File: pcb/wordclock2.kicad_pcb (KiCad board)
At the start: 2 copper layers, 130 x 30 mm, 57 parts, among them J1 Jack-DC, J2 CONN_02X05, J3 Micro_SD_Card_Det, J4 USB_OTG, J5 CONN_01X03, J6 CONN_01X03, Q1 FDS6890A, SW1 SW_Push, SW2 SW_Push, SW3 SW_Push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

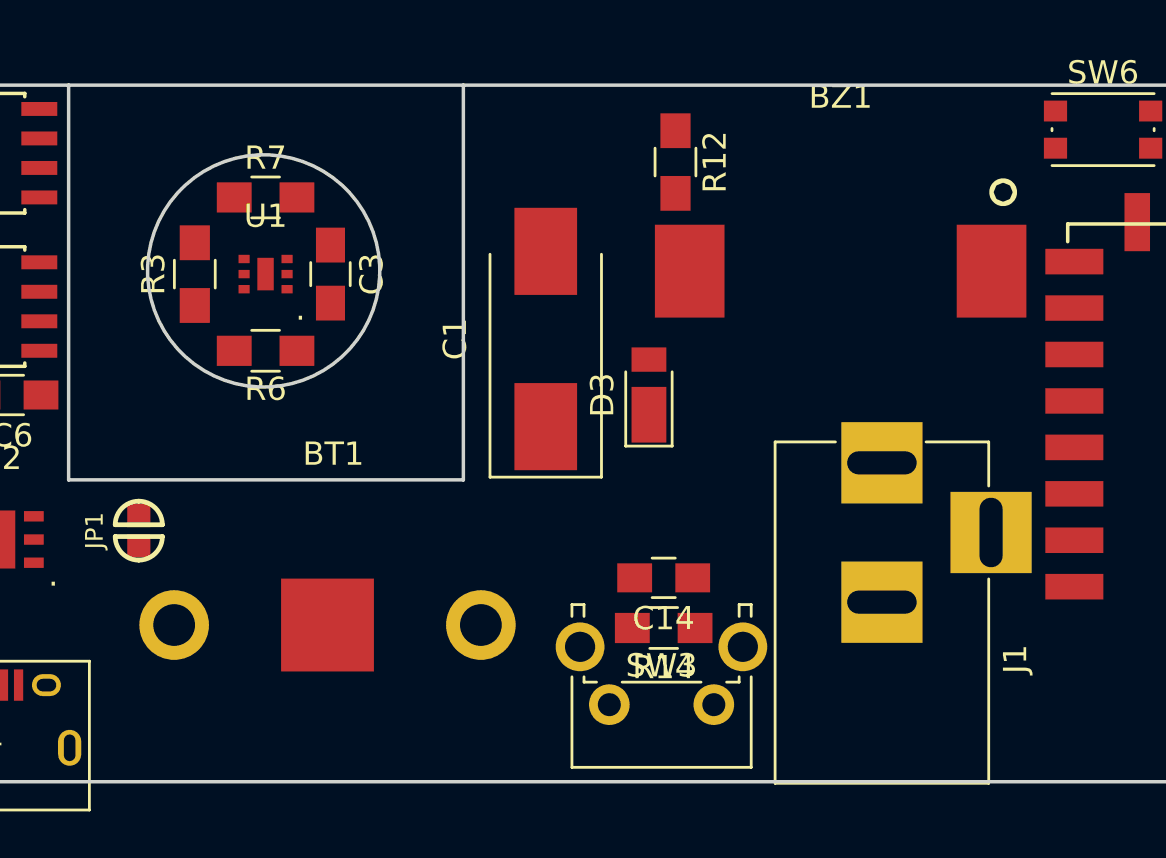
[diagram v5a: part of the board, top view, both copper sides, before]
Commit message: smaller battery mount
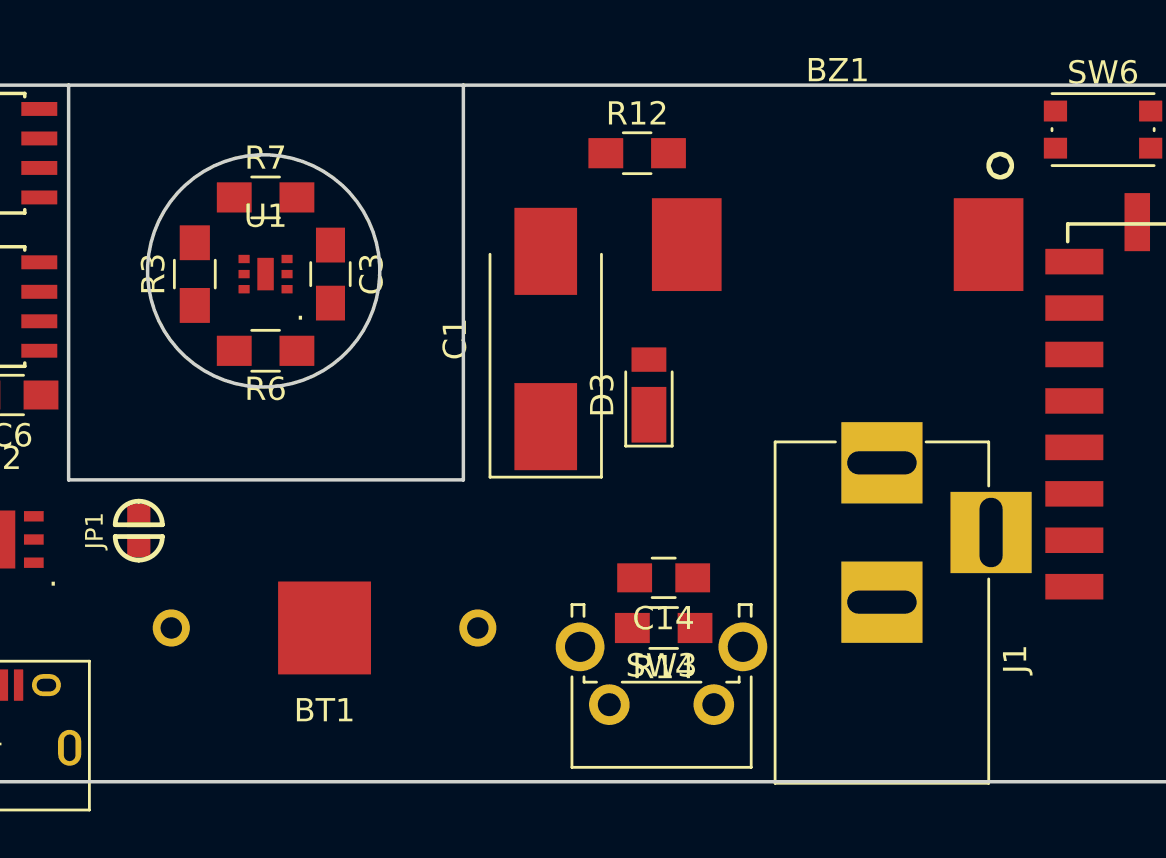
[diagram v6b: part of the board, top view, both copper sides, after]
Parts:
- BT1: footprint wordclockFB:LR44 -> wordclockFB:BK-890
- moved R12 1.69 mm to (164.1, 82.9), turned to 0 degrees
- moved BZ1 1.15 mm to (172.7, 86.9)
- moved BT1 0.18 mm to (150.6, 103.4)
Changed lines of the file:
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@@
   )
   (module wordclockFB:PKLCS1212E (layer F.Cu)
-    (at 172.847 88.011)
+    (at 172.72 86.868)
     (fp_text reference BZ1 (at 0 -7.5) (layer F.SilkS)
       (effects (font (size 1 1) (thickness 0.15)))
@@
   )
   (module Resistors_SMD:R_0805_HandSoldering (layer F.Cu)
-    (at 165.735 83.312 270)
+    (at 164.084 82.931)
     (descr "Resistor SMD 0805, hand soldering")
     (tags "resistor 0805")
     (attr smd)
-    (fp_text reference R12 (at 0 -1.7 270) (layer F.SilkS)
-      (effects (font (size 1 1) (thickness 0.15)))
-    )
-    (fp_text value 1k (at 0 1.75 270) (layer F.Fab)
-      (effects (font (size 1 1) (thickness 0.15)))
-    )
-    (fp_text user %R (at 0 0 270) (layer F.Fab)
+    (fp_text reference R12 (at 0 -1.7) (layer F.SilkS)
+      (effects (font (size 1 1) (thickness 0.15)))
+    )
+    (fp_text value 1k (at 0 1.75) (layer F.Fab)
+      (effects (font (size 1 1) (thickness 0.15)))
+    )
+    (fp_text user %R (at 0 0) (layer F.Fab)
       (effects (font (size 0.5 0.5) (thickness 0.075)))
     )
@@
     (fp_line (start 2.35 0.9) (end 2.35 -0.9) (layer F.CrtYd) (width 0.05))
     (fp_line (start 2.35 0.9) (end -2.35 0.9) (layer F.CrtYd) (width 0.05))
-    (pad 1 smd rect (at -1.35 0 270) (size 1.5 1.3) (layers F.Cu F.Paste F.Mask)
-      (net 3 +3V3))
-    (pad 2 smd rect (at 1.35 0 270) (size 1.5 1.3) (layers F.Cu F.Paste F.Mask)
+    (pad 1 smd rect (at -1.35 0) (size 1.5 1.3) (layers F.Cu F.Paste F.Mask)
+      (net 3 +3V3))
+    (pad 2 smd rect (at 1.35 0) (size 1.5 1.3) (layers F.Cu F.Paste F.Mask)
       (net 69 "Net-(BZ1-Pad1)"))
     (model ${KISYS3DMOD}/Resistors_SMD.3dshapes/R_0805.wrl
@@
     )
   )
-  (module wordclockFB:LR44 (layer F.Cu)
-    (at 150.749 103.251)
-    (fp_text reference BT1 (at 0.254 -7.366) (layer F.SilkS)
-      (effects (font (size 1 1) (thickness 0.15)))
-    )
-    (fp_text value Battery_Cell (at 0 7.874) (layer F.Fab)
-      (effects (font (size 1 1) (thickness 0.15)))
-    )
-    (fp_line (start -6.605 -6.07) (end -6.605 6.07) (layer F.Fab) (width 0.15))
-    (fp_line (start -6.605 6.07) (end 6.605 6.07) (layer F.Fab) (width 0.15))
-    (fp_line (start 6.605 6.07) (end 6.605 -6.07) (layer F.Fab) (width 0.15))
-    (fp_line (start 6.605 -6.07) (end -6.605 -6.07) (layer F.Fab) (width 0.15))
-    (pad 1 thru_hole circle (at -6.605 0) (size 3 3) (drill 1.8) (layers *.Cu *.Mask)
+  (module wordclockFB:BK-890 (layer F.Cu)
+    (at 150.622 103.378)
+    (fp_text reference BT1 (at 0 3.556) (layer F.SilkS)
+      (effects (font (size 1 1) (thickness 0.15)))
+    )
+    (fp_text value Battery_Cell (at 0 -3.556) (layer F.Fab)
+      (effects (font (size 1 1) (thickness 0.15)))
+    )
+    (fp_line (start -6.6 -6.25) (end -6.6 6.25) (layer F.Fab) (width 0.15))
+    (fp_line (start -6.6 6.25) (end 6.6 6.25) (layer F.Fab) (width 0.15))
+    (fp_line (start 6.6 6.25) (end 6.6 -6.25) (layer F.Fab) (width 0.15))
+    (fp_line (start 6.6 -6.25) (end -6.6 -6.25) (layer F.Fab) (width 0.15))
+    (pad 1 thru_hole circle (at -6.6 0) (size 1.6 1.6) (drill 0.925) (layers *.Cu *.Mask)
       (net 2 "Net-(BT1-Pad1)"))
-    (pad 1 thru_hole circle (at 6.605 0) (size 3 3) (drill 1.8) (layers *.Cu *.Mask)
+    (pad 1 thru_hole circle (at 6.6 0) (size 1.6 1.6) (drill 0.925) (layers *.Cu *.Mask)
       (net 2 "Net-(BT1-Pad1)"))
     (pad 2 smd rect (at 0 0) (size 4 4) (layers F.Cu F.Paste F.Mask)

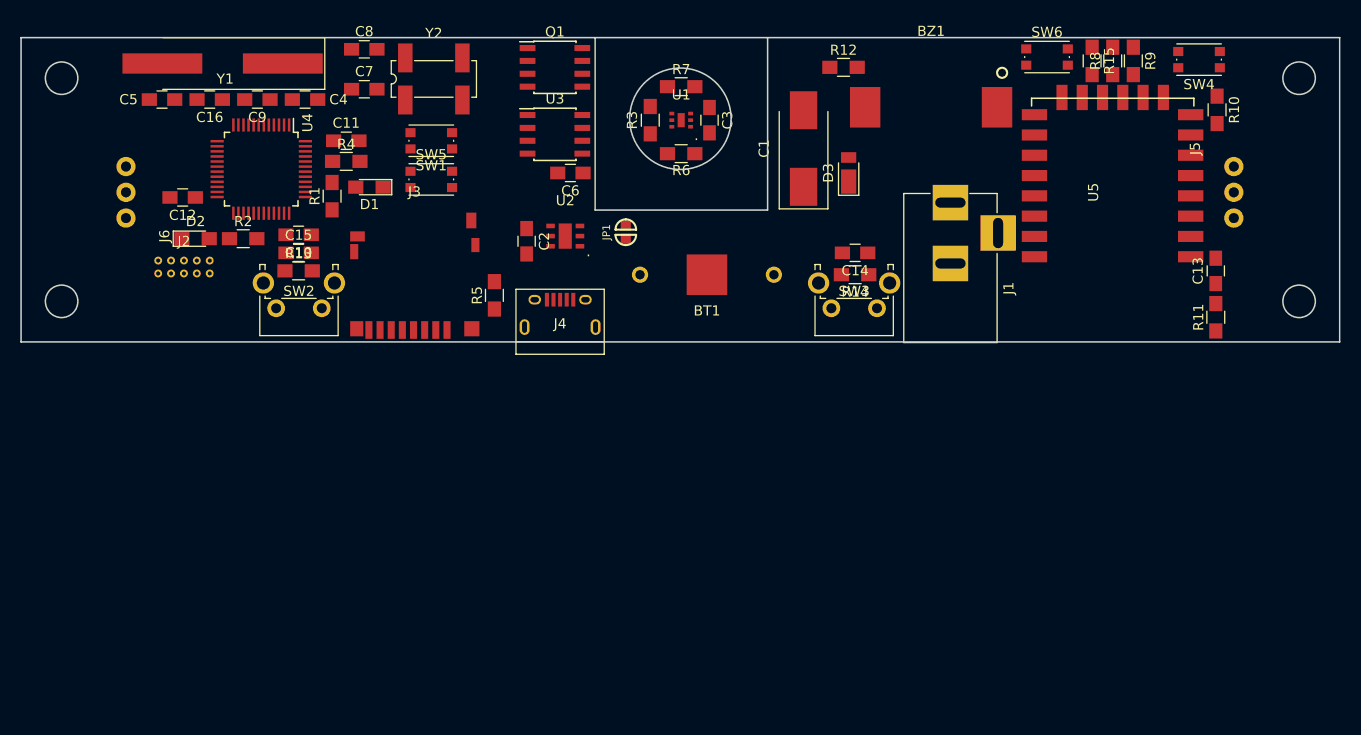
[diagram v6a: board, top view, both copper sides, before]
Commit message: changed to 0603 components, added schematic notes
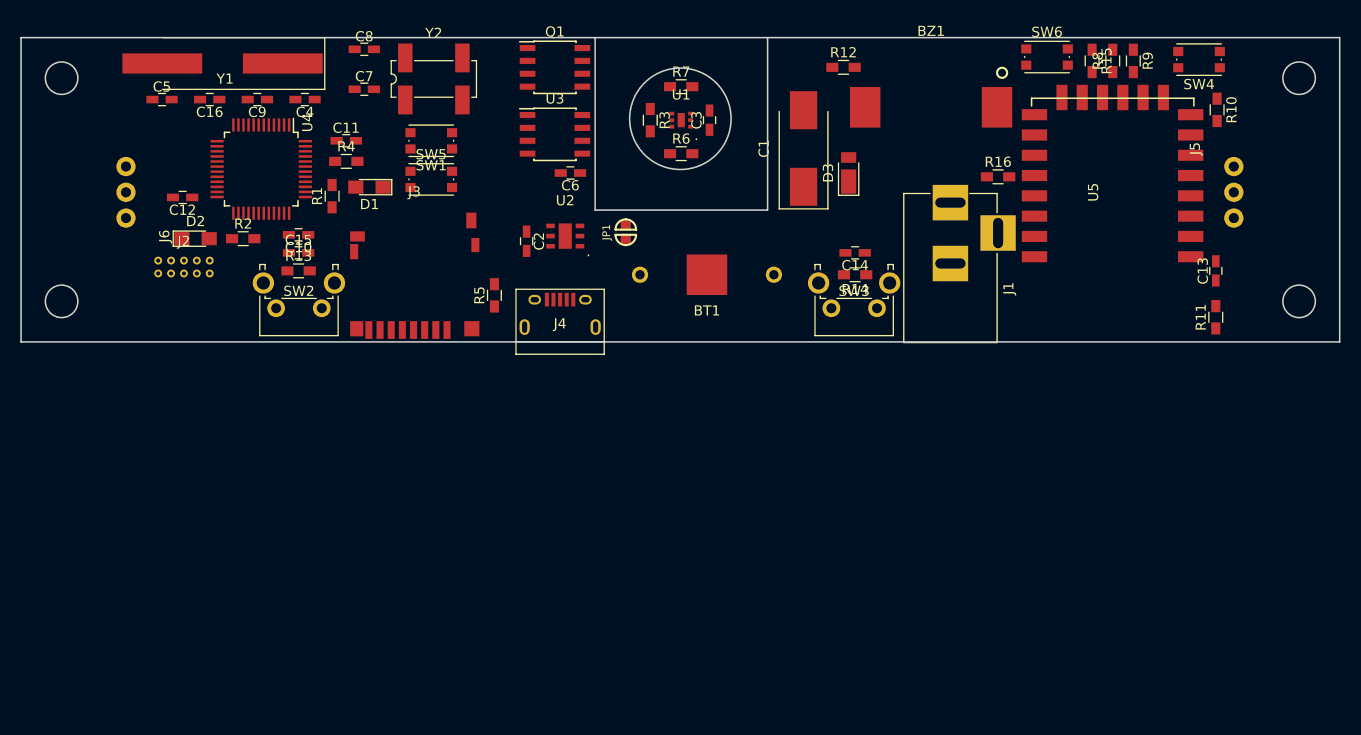
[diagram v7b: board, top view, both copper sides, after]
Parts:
- added R16: 100, Resistors_SMD:R_0603_HandSoldering, F.Cu at (179.3, 93.7)
- C10, C11, C12, C13, C14, C15, C16, C2, C3, C4, C5, C6, C7, C8, C9: footprint Capacitors_SMD:C_0805_HandSoldering -> Capacitors_SMD:C_0603_HandSoldering
- R1, R10, R11, R12, R13, R14, R15, R2, R3, R4, R5, R6, R7, R8, R9: footprint Resistors_SMD:R_0805_HandSoldering -> Resistors_SMD:R_0603_HandSoldering
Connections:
- U4 pad 26: /ESP_GPIO0 -> Net-(R16-Pad1)
- U4 pad 38: Net-(U4-Pad38) -> /PA15
- U5 pad 14: Net-(U5-Pad14) -> /PA15

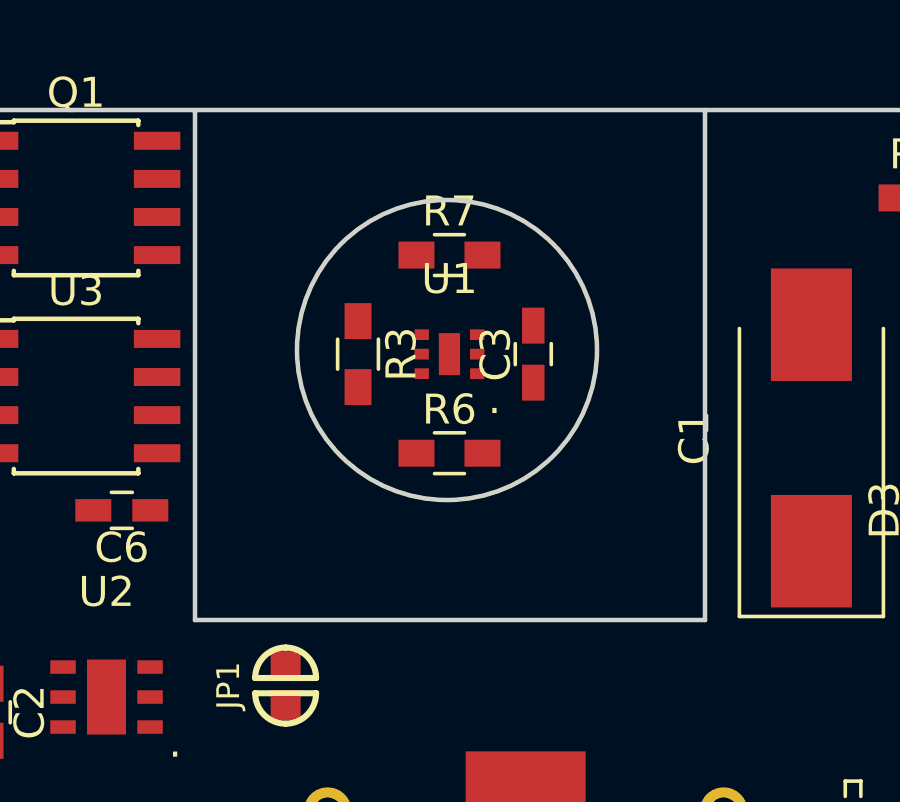
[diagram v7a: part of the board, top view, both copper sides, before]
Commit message: drawing notes, moved hole lines to fab layer
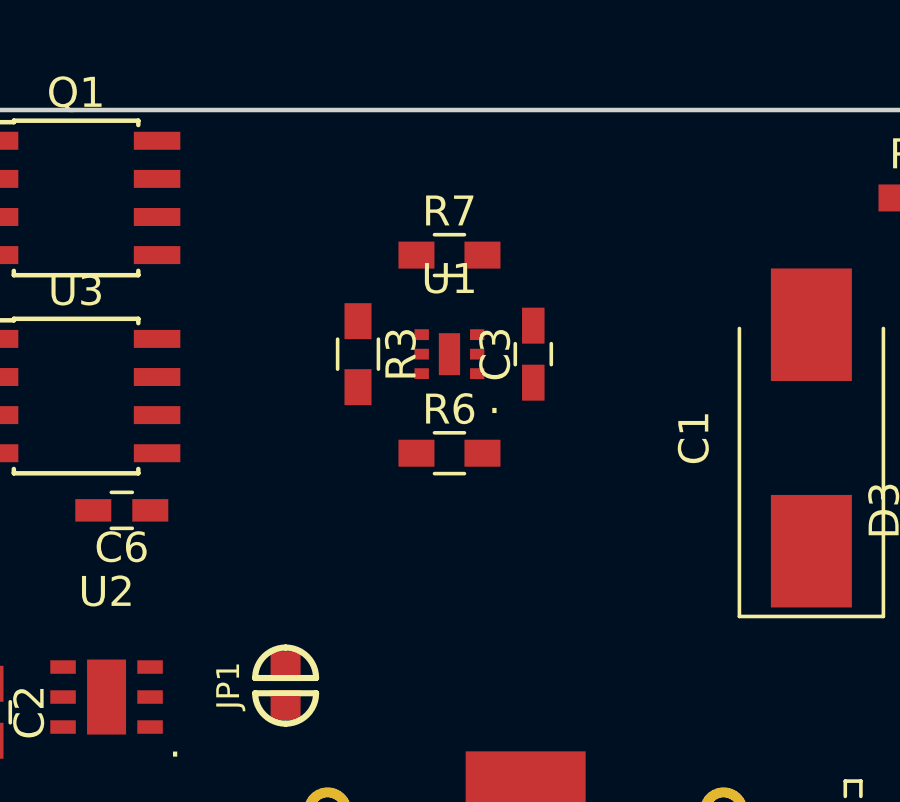
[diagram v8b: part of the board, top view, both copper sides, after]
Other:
- outline, holes or cut-outs redrawn
- board text added: "Aussparung Gehäuse (mit Loch für Lichtsensor; s. 3D Model)"
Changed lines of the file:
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@@
     (area 82.924999 79.924999 213.075001 110.075001)
     (thickness 1.6)
-    (drawings 12)
+    (drawings 13)
     (tracks 0)
     (zones 0)
@@
     (zone_45_only no)
     (trace_min 0.2)
-    (segment_width 0.2)
+    (segment_width 0.15)
     (edge_width 0.15)
     (via_size 0.6)
@@
     )
   )
-  (gr_line (start 156.6 97) (end 156.6 80) (angle 90) (layer Edge.Cuts) (width 0.15))
-  (gr_line (start 139.6 97) (end 156.6 97) (angle 90) (layer Edge.Cuts) (width 0.15))
-  (gr_line (start 139.6 80) (end 139.6 97) (angle 90) (layer Edge.Cuts) (width 0.15))
-  (gr_circle (center 148 88) (end 153 88) (layer Edge.Cuts) (width 0.15))
+  (gr_text "Aussparung Gehäuse\n(mit Loch für Lichtsensor; s. 3D Model)" (at 148.209 77.343) (layer F.Fab)
+    (effects (font (size 1 1) (thickness 0.2)))
+  )
+  (gr_line (start 156.6 97) (end 156.6 80) (angle 90) (layer F.Fab) (width 0.15))
+  (gr_line (start 139.6 97) (end 156.6 97) (angle 90) (layer F.Fab) (width 0.15))
+  (gr_line (start 139.6 80) (end 139.6 97) (angle 90) (layer F.Fab) (width 0.15))
+  (gr_circle (center 148 88) (end 153 88) (layer F.Fab) (width 0.15))
   (gr_circle (center 209 106) (end 210.6 106) (layer Edge.Cuts) (width 0.15))
   (gr_circle (center 209 84) (end 210.6 84) (layer Edge.Cuts) (width 0.15))
